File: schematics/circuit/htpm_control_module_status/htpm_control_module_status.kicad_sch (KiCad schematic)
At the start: 34 parts, among them J1 Conn_01x08_Socket, J2 Conn_01x04_Socket

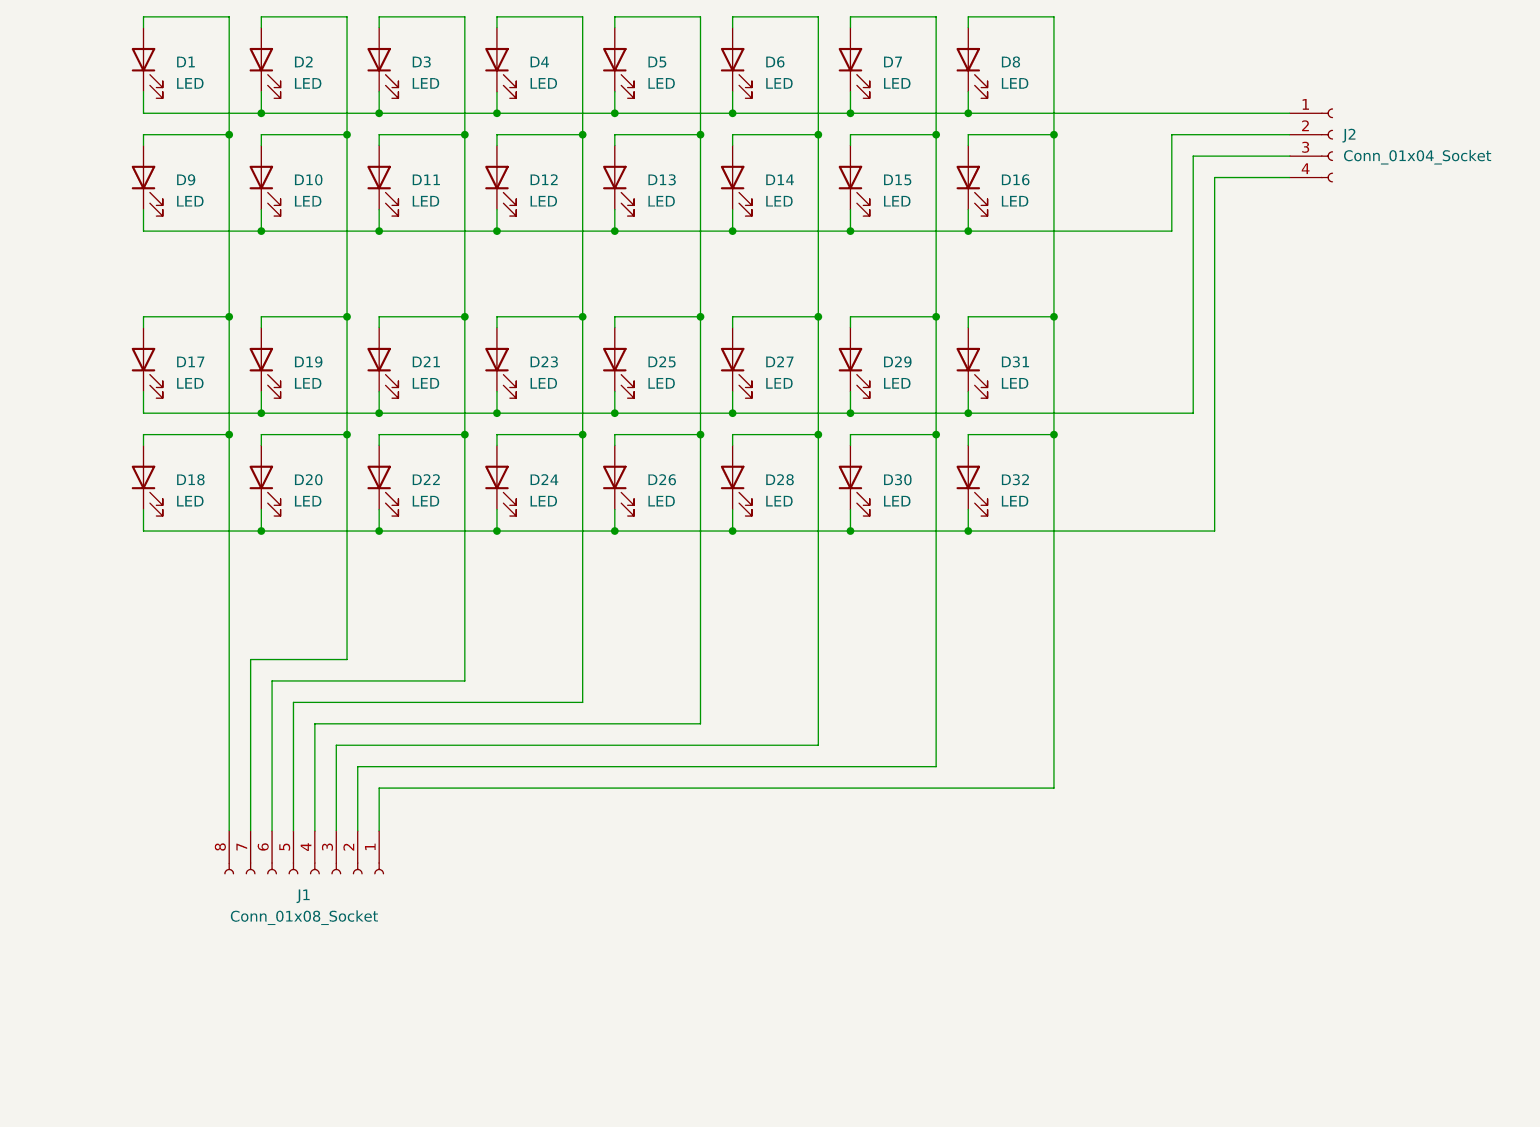
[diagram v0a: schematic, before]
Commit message: Created HTPm CONTROL Module Status PCB.
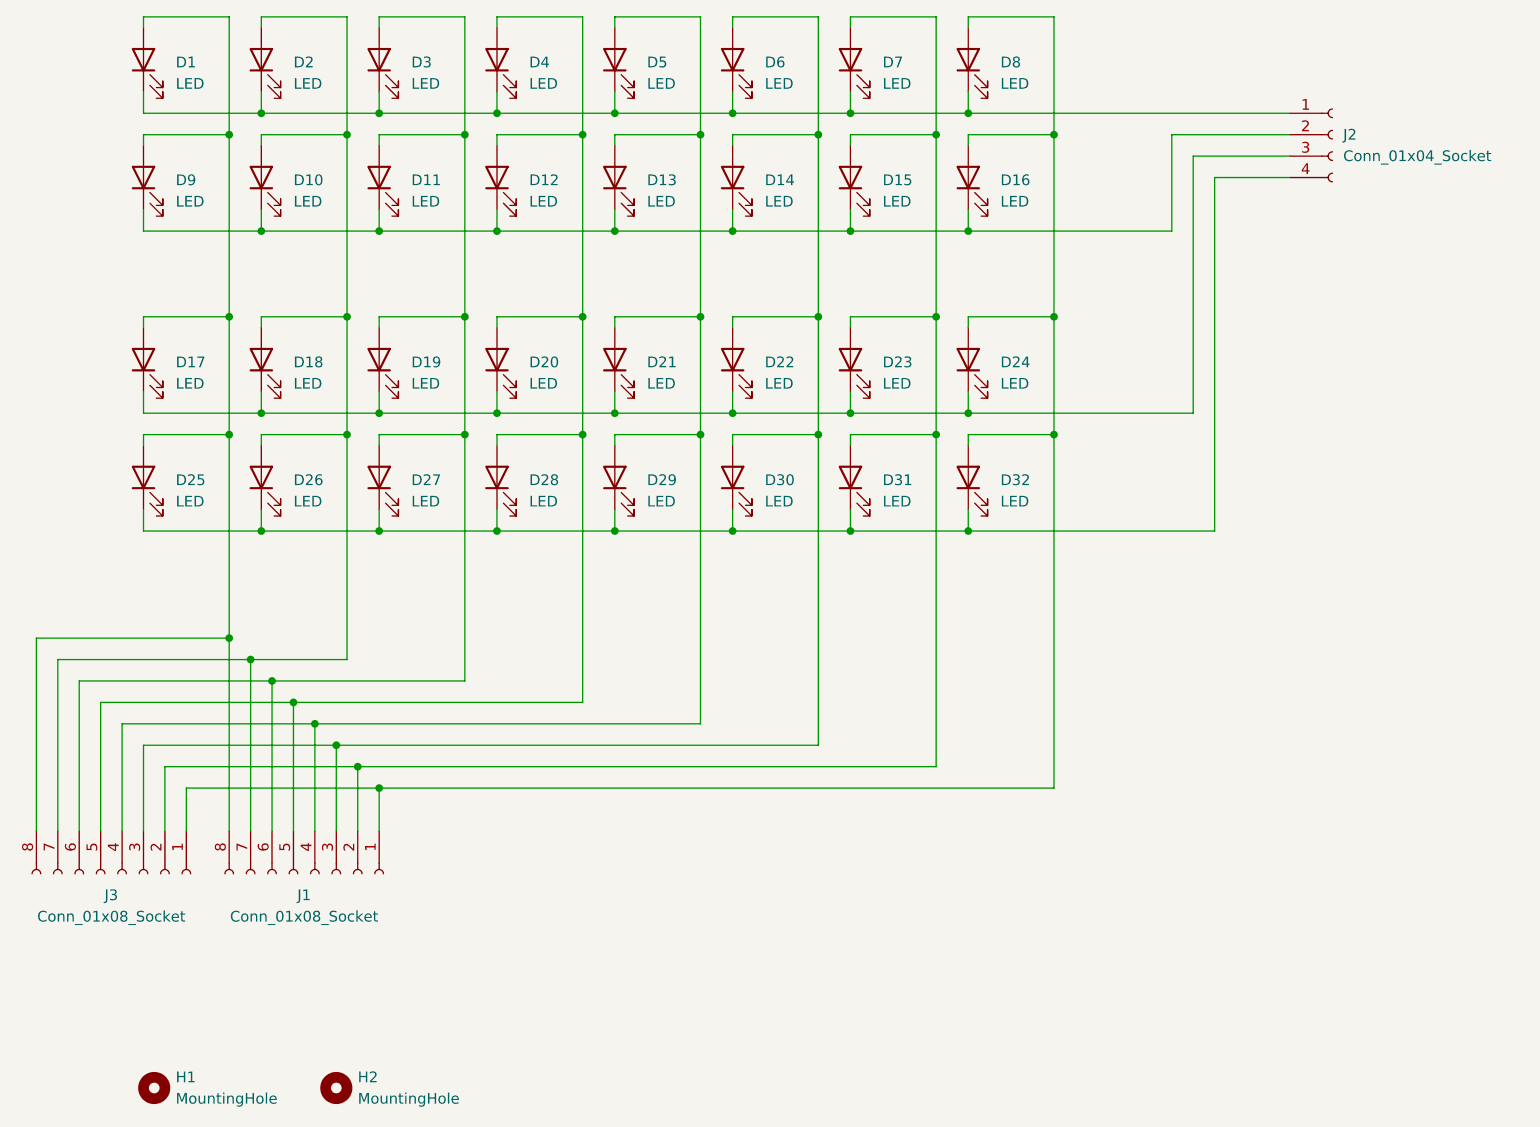
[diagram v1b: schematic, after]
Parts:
- added H1, H2: MountingHole, MountingHole:MountingHole_2.5mm, symbol Mechanical:MountingHole
- added J3: Conn_01x08_Socket, Connector_PinHeader_2.00mm:PinHeader_1x08_P2.00mm_Vertical, symbol Connector:Conn_01x08_Socket
- D1, D10, D11, D12, D13, D14, D15, D16, D17, D18, D19, D2, D20, D21, D22, D23, D24, D25, D26, D27, D28, D29, D3, D30, D31, D32, D4, D5, D6, D7, D8, D9: footprint (none) -> LED_THT:LED_D5.0mm
- J1: footprint (none) -> Connector_PinHeader_2.00mm:PinHeader_1x08_P2.00mm_Vertical
- J2: footprint (none) -> Connector_PinHeader_2.00mm:PinHeader_1x04_P2.00mm_Vertical
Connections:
- net at D17.1 (K), D19.1 (K), D21.1 (K)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: now also D18.1 (K), D20.1 (K), D22.1 (K), D24.1 (K); no longer D25.1 (K), D27.1 (K), D29.1 (K), D31.1 (K)
- net at D11.2 (A), D3.2 (A), J1.6 (Pin_6): now also D19.2 (A), D27.2 (A), J3.6 (Pin_6); no longer D21.2 (A), D22.2 (A)
- net at D1.2 (A), D17.2 (A), D9.2 (A)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: now also D25.2 (A), J3.8 (Pin_8); no longer D18.2 (A)
- net at D10.2 (A), D2.2 (A), J1.7 (Pin_7): now also D18.2 (A), D26.2 (A), J3.7 (Pin_7); no longer D19.2 (A), D20.2 (A)
- net at D26.1 (K), D28.1 (K), D30.1 (K)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: now also D25.1 (K), D27.1 (K), D29.1 (K), D31.1 (K); no longer D18.1 (K), D20.1 (K), D22.1 (K), D24.1 (K)
- net at D13.2 (A), D5.2 (A), J1.4 (Pin_4): now also D21.2 (A), D29.2 (A), J3.4 (Pin_4); no longer D25.2 (A), D26.2 (A)
- net at D15.2 (A), D7.2 (A), J1.2 (Pin_2): now also D23.2 (A), D31.2 (A), J3.2 (Pin_2); no longer D29.2 (A), D30.2 (A)
- net at D12.2 (A), D4.2 (A), J1.5 (Pin_5): now also D20.2 (A), D28.2 (A), J3.5 (Pin_5); no longer D23.2 (A), D24.2 (A)
- net at D16.2 (A), D32.2 (A), D8.2 (A)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: now also D24.2 (A), J3.1 (Pin_1); no longer D31.2 (A)
- net at D14.2 (A), D6.2 (A), J1.3 (Pin_3): now also D22.2 (A), D30.2 (A), J3.3 (Pin_3); no longer D27.2 (A), D28.2 (A)
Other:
- moved on the sheet: D18, D19, D20, D21, D22, D23, D24, D25, D26, D27, D28, D29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

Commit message: Updated nominal values.
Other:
- note added: "DIG"
- note added: "SEG"
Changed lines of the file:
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@@
     (stroke (width 0) (type default))
   )
+  (text "SEG" (at 92.71 151.13 0)
+    (effects (font (size 1.27 1.27)) (justify left bottom))
+  )
+  (text "DIG" (at 217.17 62.23 0)
+    (effects (font (size 1.27 1.27)) (justify left bottom))
+  )
+  (text "SEG" (at 69.85 151.13 0)
+    (effects (font (size 1.27 1.27)) (justify left bottom))
+  )
   (symbol (lib_id "Device:LED") (at 130.81 86.36 90) (unit 1)
     (in_bom yes) (on_board yes) (dnp no) (fields_autoplaced)
@@
   )
   (symbol (lib_id "Connector:Conn_01x08_Socket") (at 72.39 147.32 270) (unit 1)
-    (in_bom yes) (on_board yes) (dnp no) (fields_autoplaced)
-    (property "Reference" "J3" (at 71.12 149.86 90)
+    (in_bom yes) (on_board yes) (dnp no)
+    (property "Reference" "J3" (at 72.39 153.67 90)
       (effects (font (size 1.27 1.27)))
     )
-    (property "Value" "Conn_01x08_Socket" (at 71.12 152.4 90)
+    (property "Value" "Conn_01x08_Socket" (at 72.39 156.21 90)
       (effects (font (size 1.27 1.27)))
     )
@@
   )
   (symbol (lib_id "Connector:Conn_01x08_Socket") (at 95.25 147.32 270) (unit 1)
-    (in_bom yes) (on_board yes) (dnp no) (fields_autoplaced)
-    (property "Reference" "J1" (at 93.98 149.86 90)
+    (in_bom yes) (on_board yes) (dnp no)
+    (property "Reference" "J1" (at 95.25 153.67 90)
       (effects (font (size 1.27 1.27)))
     )
-    (property "Value" "Conn_01x08_Socket" (at 93.98 152.4 90)
+    (property "Value" "Conn_01x08_Socket" (at 95.25 156.21 90)
       (effects (font (size 1.27 1.27)))
     )
@@
   )
   (symbol (lib_id "Connector:Conn_01x04_Socket") (at 215.9 59.69 0) (unit 1)
-    (in_bom yes) (on_board yes) (dnp no) (fields_autoplaced)
-    (property "Reference" "J2" (at 217.17 59.69 0)
+    (in_bom yes) (on_board yes) (dnp no)
+    (property "Reference" "J2" (at 217.17 53.34 0)
       (effects (font (size 1.27 1.27)) (justify left))
     )
-    (property "Value" "Conn_01x04_Socket" (at 217.17 62.23 0)
+    (property "Value" "Conn_01x04_Socket" (at 217.17 55.88 0)
       (effects (font (size 1.27 1.27)) (justify left))
     )
